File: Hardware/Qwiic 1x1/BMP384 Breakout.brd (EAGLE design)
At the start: 25.4 x 25.4 mm, 48 parts, among them J1 QWIIC_RIGHT_ANGLE, J2 QWIIC_RIGHT_ANGLE, U1 BMP384

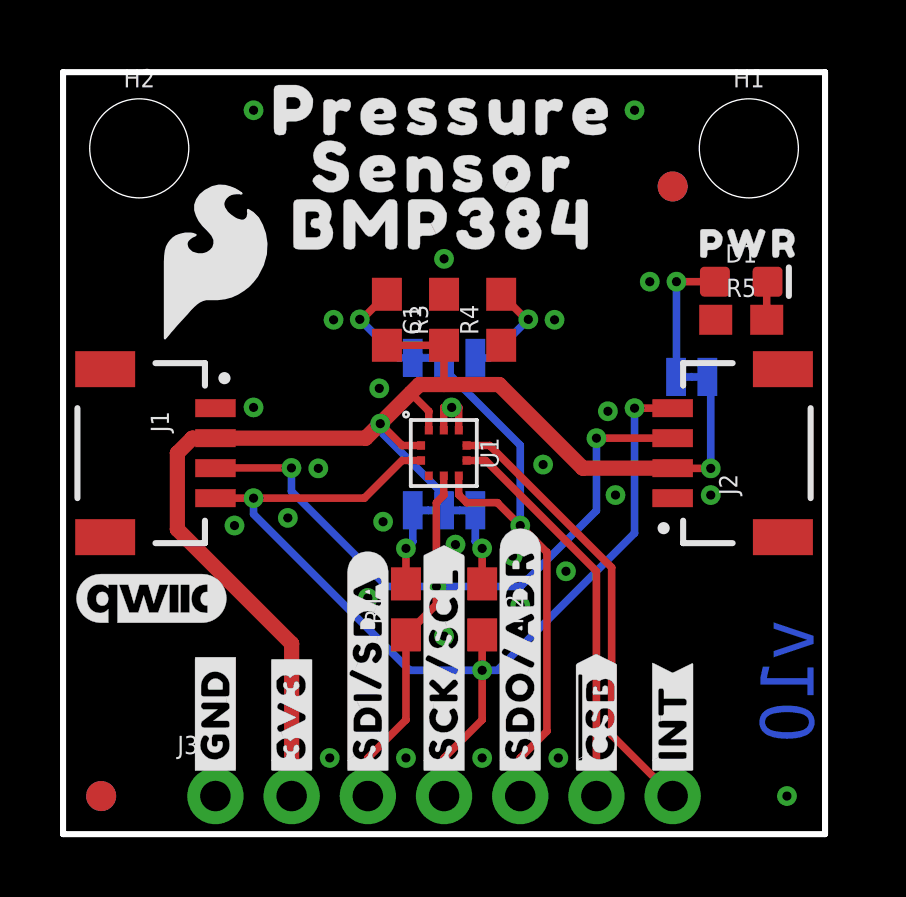
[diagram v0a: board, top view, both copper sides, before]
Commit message: Remove library file
BMP384 is in SFE Eagle library, update part in design
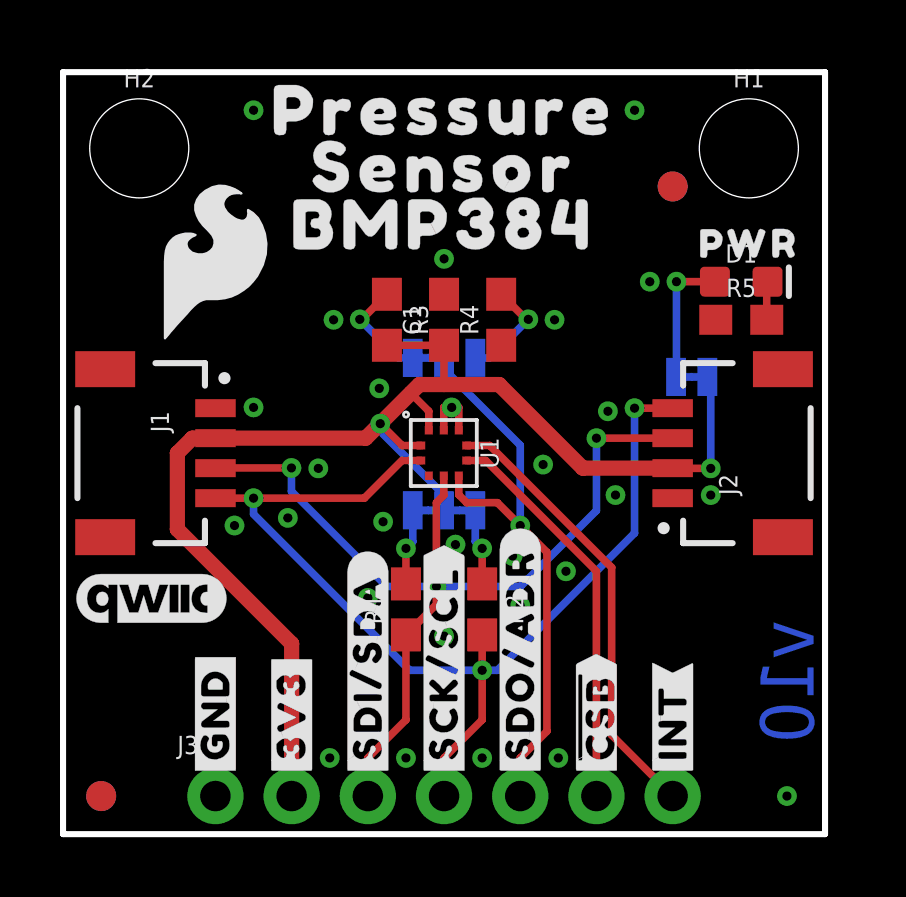
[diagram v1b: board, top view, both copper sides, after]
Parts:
- U1: device bmp384:LGA-10 -> SparkFun-Sensors:LGA-10
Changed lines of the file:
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@@
 <attribute name="REV" value="" x="-8.89" y="-13.97" size="1.778" layer="27" font="vector" ratio="15" display="off"/>
 </element>
-<element name="U1" library="bmp384" package="LGA-10" value="BMP384" x="12.691" y="12.7045" smashed="yes" rot="R90">
+<element name="U1" library="SparkFun-Sensors" package="LGA-10" value="BMP384" x="12.691" y="12.7045" smashed="yes" rot="R90">
 <attribute name="NAME" x="14.215" y="12.7045" size="0.6096" layer="25" font="vector" ratio="20" rot="R90" align="center"/>
 <attribute name="PROD_ID" value="IC-16677" x="12.691" y="12.7045" size="1.778" layer="27" ratio="15" rot="R90" display="off"/>
